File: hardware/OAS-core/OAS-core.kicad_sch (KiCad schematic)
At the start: 9 parts, among them J1 Micro_SD_Card, J2 PROG, J3 MSC, J4 Conn_01x02_Pin, U1 ESP32-WROOM-32, U2 TPS2116DRL/TPS2117, U3 TPS54336ADDA, U5 TPS563202DRLR

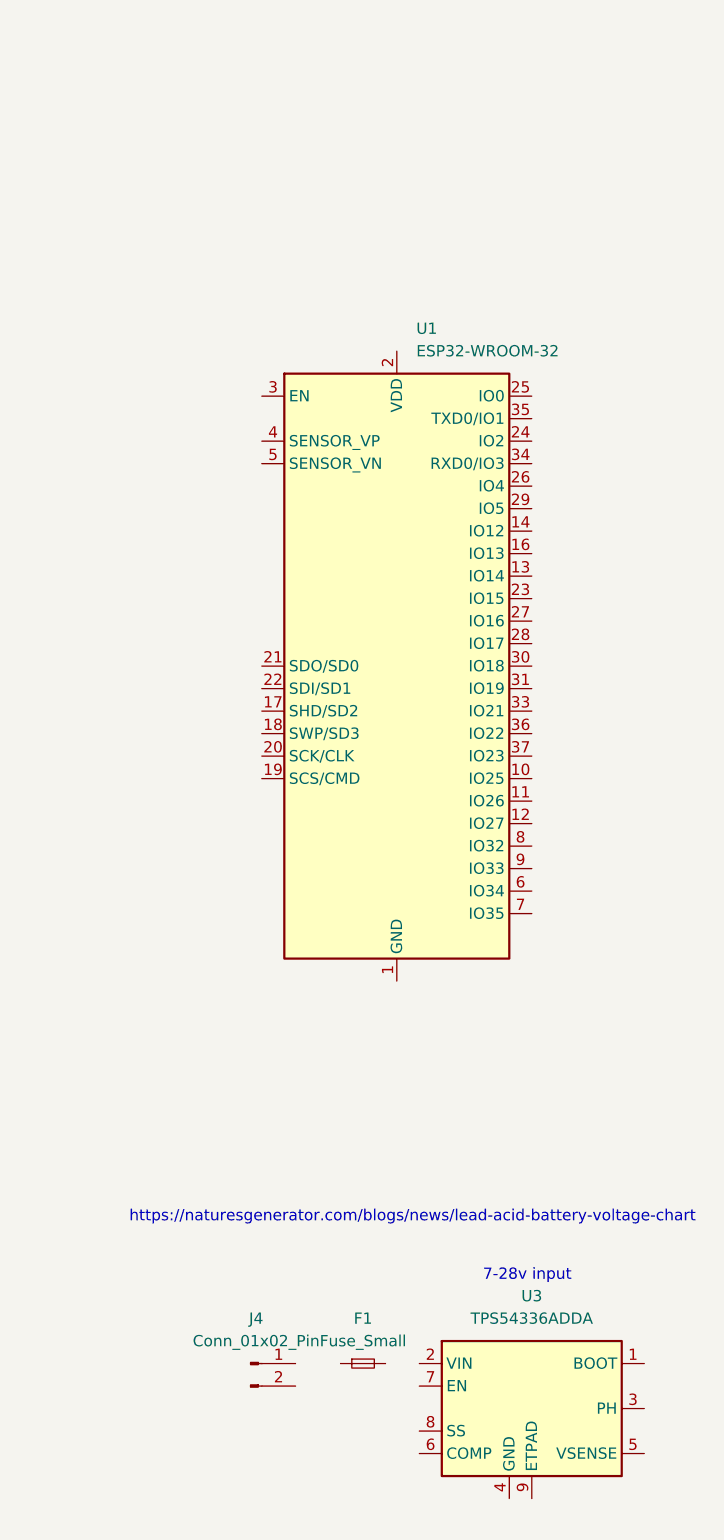
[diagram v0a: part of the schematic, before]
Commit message: Spec input protection
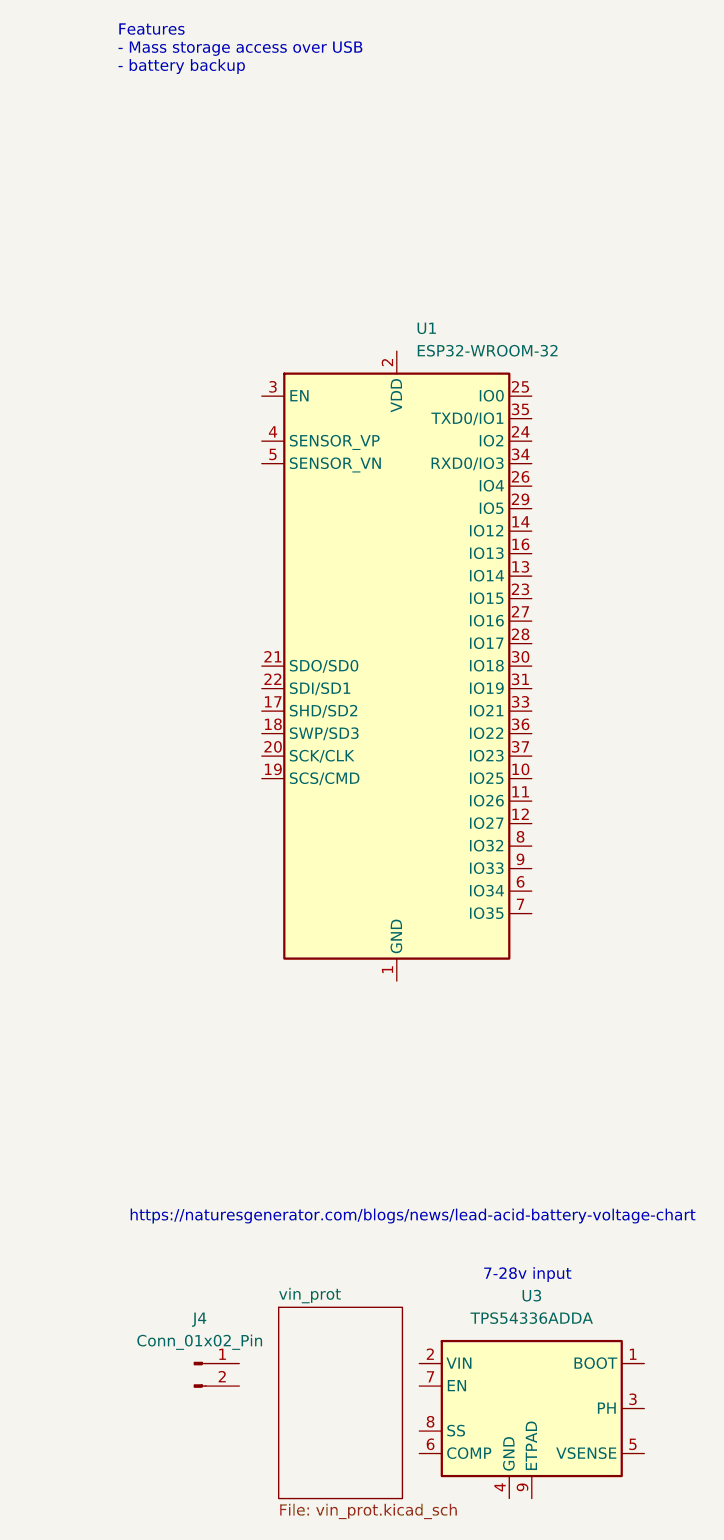
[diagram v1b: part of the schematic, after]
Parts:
- removed F1: Fuse_Small, symbol Device:Fuse_Small
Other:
- added sheet vin_prot (vin_prot.kicad_sch)
- note added: "Features - Mass storage access over USB - battery backup"
- moved on the sheet: J4
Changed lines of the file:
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@@
+		)
+	)
+	(text "Features\n- Mass storage access over USB\n- battery backup\n"
+		(exclude_from_sim no)
+		(at 14.224 15.494 0)
+		(effects
+			(font
+				(size 1.27 1.27)
+			)
+			(justify left)
 		)
 	)
@@
 	)
 	(symbol
-		(lib_id "Device:Fuse_Small")
-		(at 41.91 163.83 0)
+		(lib_id "Connector:Conn_01x02_Pin")
+		(at 22.86 163.83 0)
 		(unit 1)
 		(exclude_from_sim no)
@@
 		(dnp no)
 		(fields_autoplaced yes)
-		(property "Reference" "F1"
-			(at 41.91 158.75 0)
-			(effects
-				(font
-					(size 1.27 1.27)
-				)
-			)
-		)
-		(property "Value" "Fuse_Small"
-			(at 41.91 161.29 0)
+		(property "Reference" "J4"
+			(at 23.495 158.75 0)
+			(effects
+				(font
+					(size 1.27 1.27)
+				)
+			)
+		)
+		(property "Value" "Conn_01x02_Pin"
+			(at 23.495 161.29 0)
 			(effects
 				(font
@@
 		)
 		(property "Footprint" ""
-			(at 41.91 163.83 0)
+			(at 22.86 163.83 0)
 			(effects
 				(font
@@
 		)
 		(property "Datasheet" "~"
-			(at 41.91 163.83 0)
-			(effects
-				(font
-					(size 1.27 1.27)
-				)
-				(hide yes)
-			)
-		)
-		(property "Description" "Fuse, small symbol"
-			(at 41.91 163.83 0)
-			(effects
-				(font
-					(size 1.27 1.27)
-				)
-				(hide yes)
-			)
-		)
-		(pin "2"
-		)
-		(pin "1"
-		)
-		(instances
-			(project ""
-				(path "/f7d13605-8f23-4146-b126-39b6825b1393"
-					(reference "F1")
-					(unit 1)
-				)
-			)
-		)
-	)
-	(symbol
-		(lib_id "Connector:Conn_01x02_Pin")
-		(at 29.21 163.83 0)
-		(unit 1)
-		(exclude_from_sim no)
-		(in_bom yes)
-		(on_board yes)
-		(dnp no)
-		(fields_autoplaced yes)
-		(property "Reference" "J4"
-			(at 29.845 158.75 0)
-			(effects
-				(font
-					(size 1.27 1.27)
-				)
-			)
-		)
-		(property "Value" "Conn_01x02_Pin"
-			(at 29.845 161.29 0)
-			(effects
-				(font
-					(size 1.27 1.27)
-				)
-			)
-		)
-		(property "Footprint" ""
-			(at 29.21 163.83 0)
-			(effects
-				(font
-					(size 1.27 1.27)
-				)
-				(hide yes)
-			)
-		)
-		(property "Datasheet" "~"
-			(at 29.21 163.83 0)
+			(at 22.86 163.83 0)
 			(effects
 				(font
@@
 		)
 		(property "Description" "Generic connector, single row, 01x02, script generated"
-			(at 29.21 163.83 0)
+			(at 22.86 163.83 0)
 			(effects
 				(font
@@
 				)
 			)
+		)
+	)
+	(sheet
+		(at 32.385 157.48)
+		(size 13.97 21.59)
+		(fields_autoplaced yes)
+		(stroke
+			(width 0.1524)
+			(type solid)
+		)
+		(fill
+			(color 0 0 0 0.0000)
+		)
+		(property "Sheetname" "vin_prot"
+			(at 32.385 156.7684 0)
+			(effects
+				(font
+					(size 1.27 1.27)
+				)
+				(justify left bottom)
+			)
+		)
+		(property "Sheetfile" "vin_prot.kicad_sch"
+			(at 32.385 179.6546 0)
+			(effects
+				(font
+					(size 1.27 1.27)
+				)
+				(justify left top)
+			)
+		)
+		(instances
+			(project "OAS-core"
+				(path "/f7d13605-8f23-4146-b126-39b6825b1393"
+					(page "2")
+				)
+			)
